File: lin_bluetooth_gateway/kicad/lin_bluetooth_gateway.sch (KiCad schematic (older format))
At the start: 9 parts, among them P1 MOLEX-0431603103, P2 MOLEX-0431603103, P4 CONN_01X03, U1 MCP2050, U2 BL652

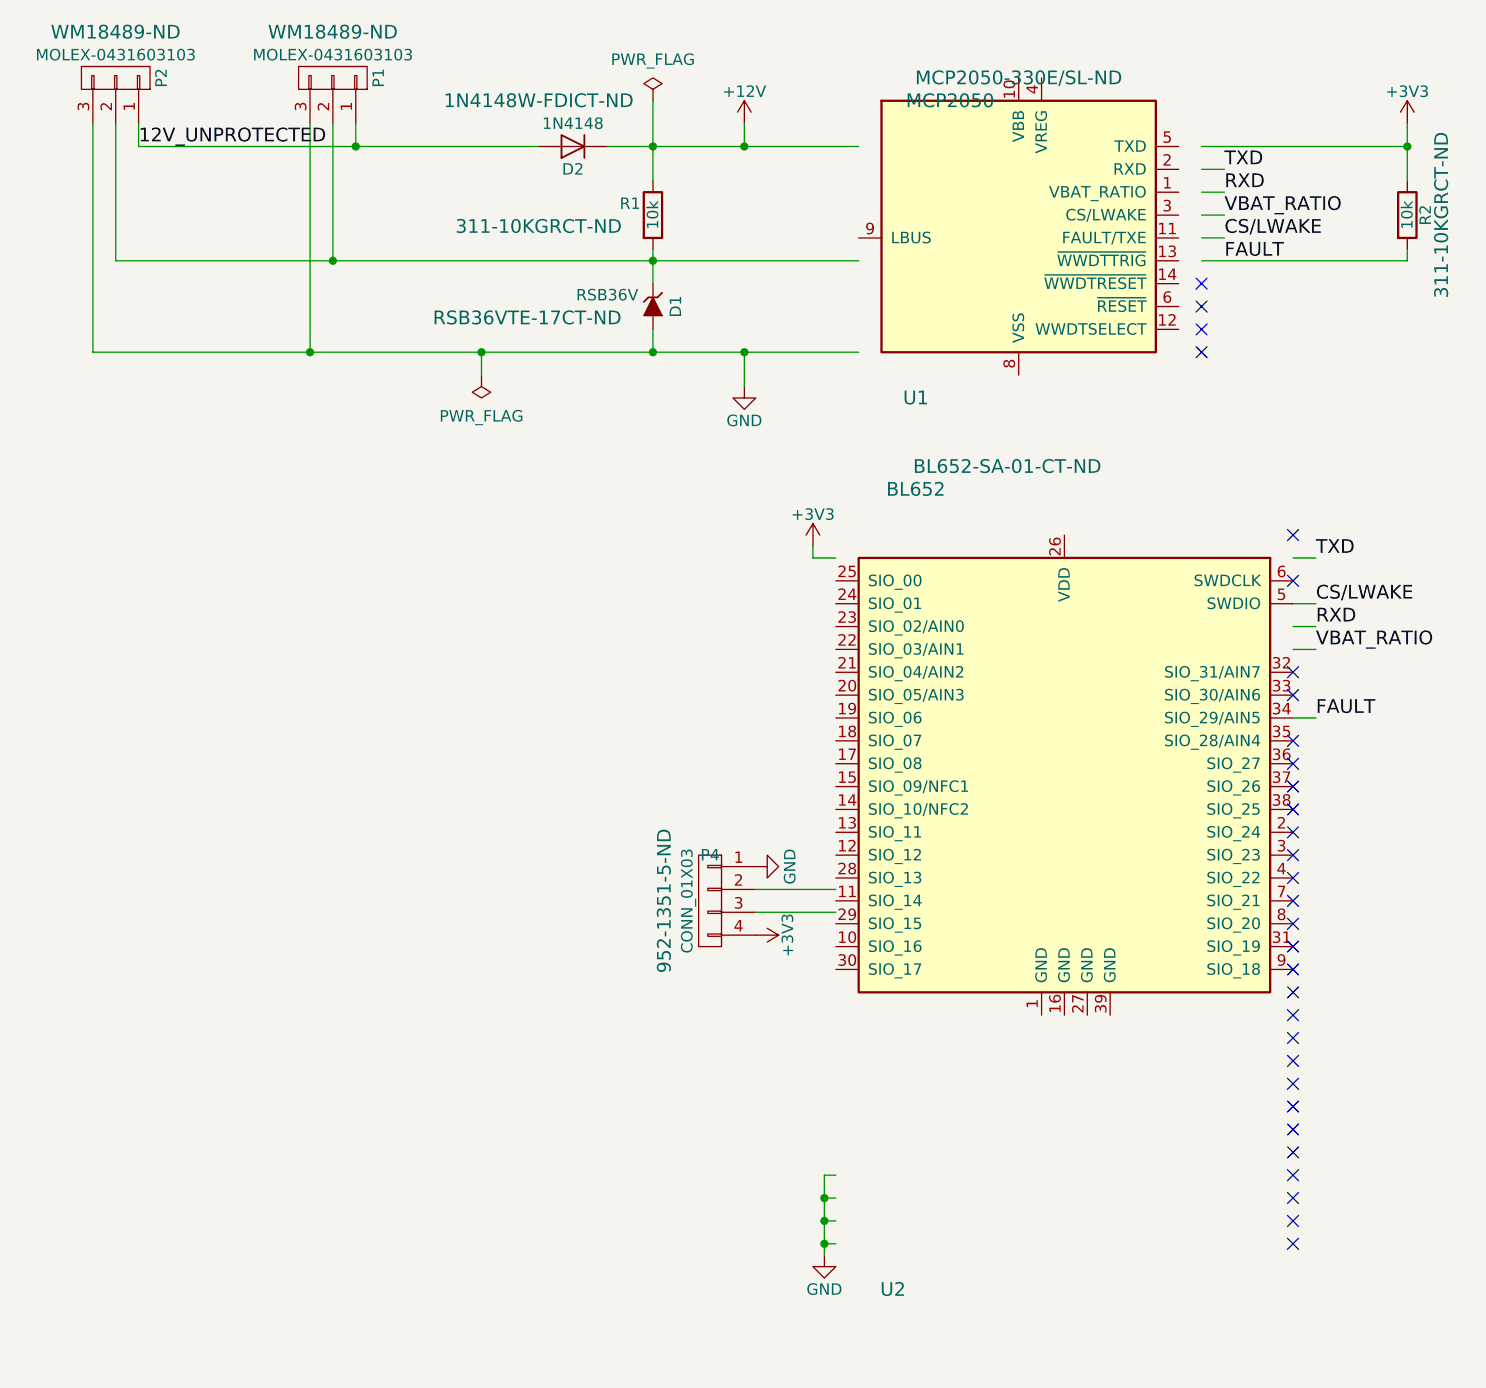
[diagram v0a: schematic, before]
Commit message: Refactoring directories
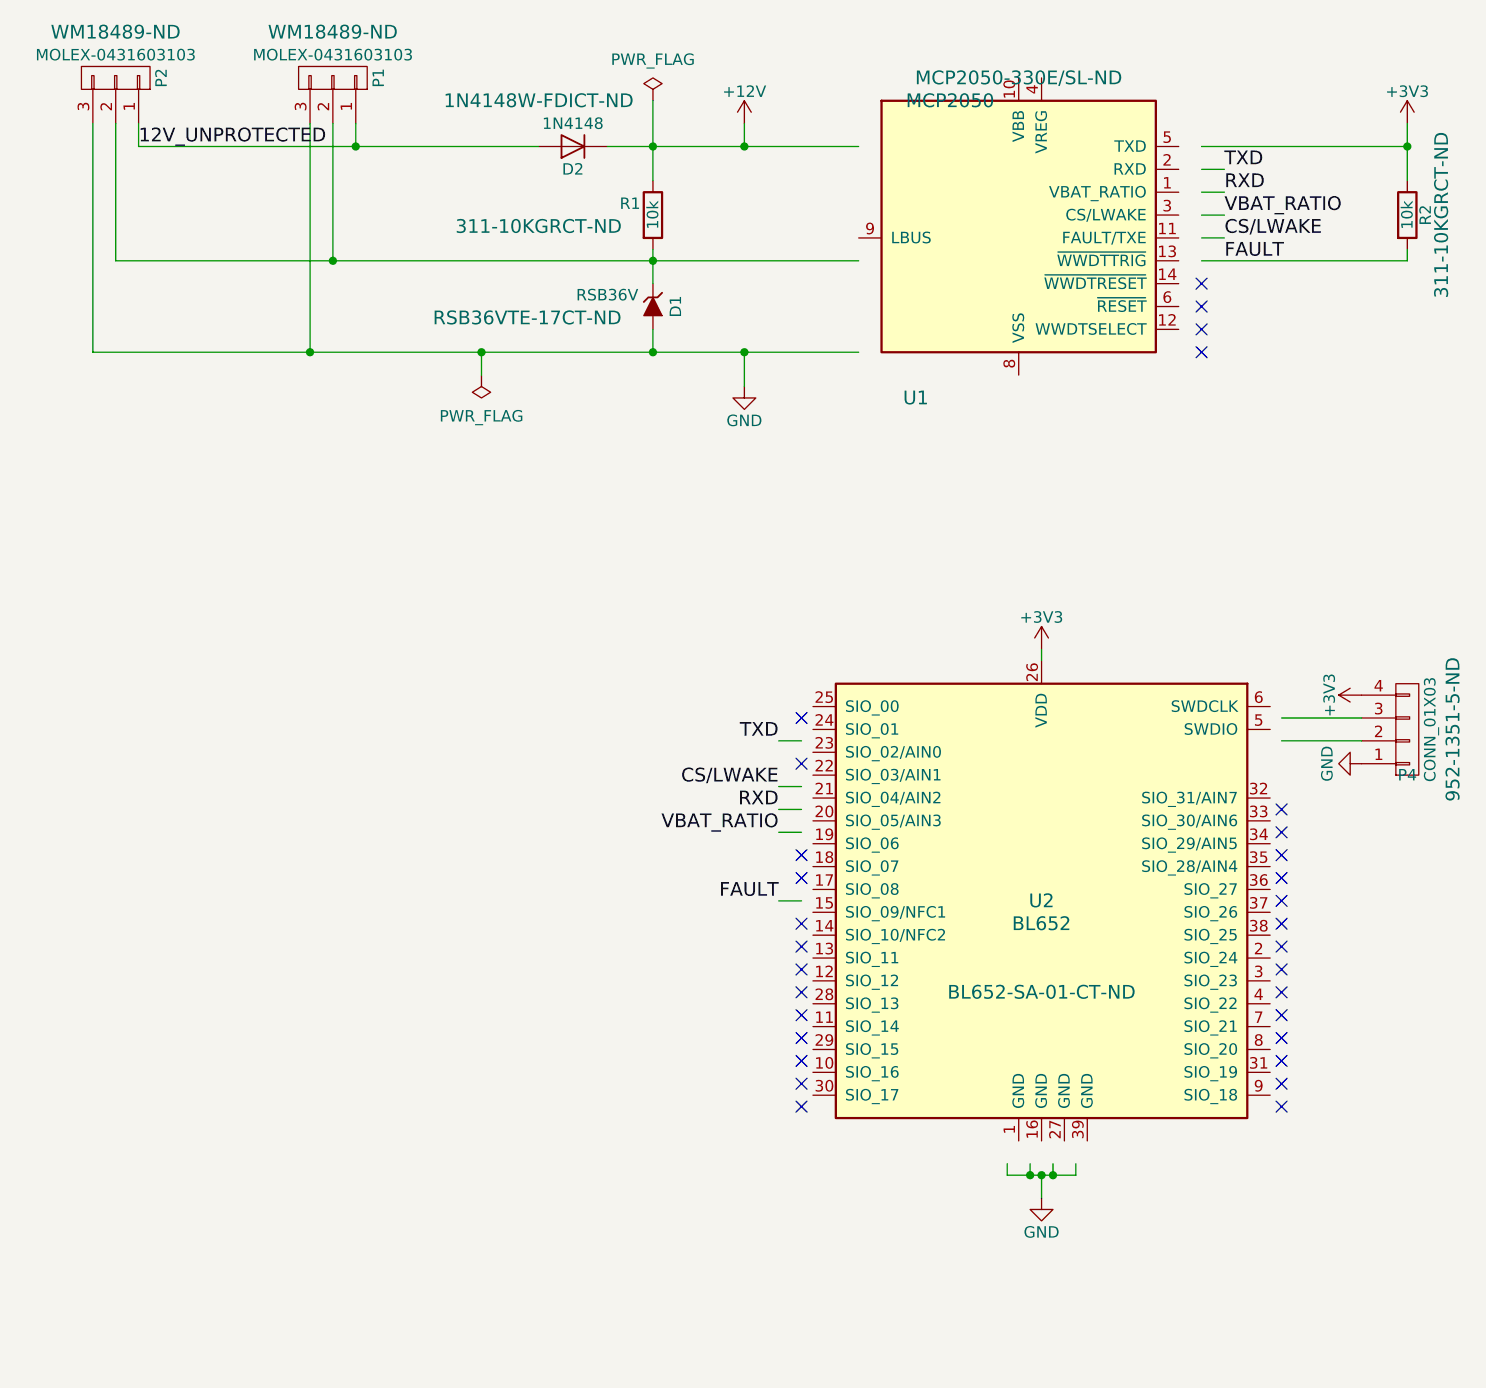
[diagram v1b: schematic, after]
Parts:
- U2: footprint footprints:BL652-SA -> Bluetooth_Modules:Bluetooth_Module_Laird_BL652
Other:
- moved on the sheet: P4, U2
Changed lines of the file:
@@
 LIBS:contrib
 LIBS:valves
-LIBS:bl652
+LIBS:laird
 LIBS:mcp2050
 LIBS:lin_bluetooth_gateway-cache
@@
 L BL652 U2
 U 1 1 5807152B
-P 5550 4250
-F 0 "U2" H 4800 2050 60  0000 C CNN
-F 1 "BL652" H 4900 5550 60  0000 C CNN
-F 2 "footprints:BL652-SA" H 5550 4250 60  0001 C CNN
-F 3 "" H 5550 4250 60  0001 C CNN
-F 4 "BL652-SA-01-CT-ND" H 5300 5650 60  0000 C CNN "DIGIKEY"
-	1    5550 4250
+P 5450 4800
+F 0 "U2" H 5450 4850 60  0000 C CNN
+F 1 "BL652" H 5450 4750 60  0000 C CNN
+F 2 "Bluetooth_Modules:Bluetooth_Module_Laird_BL652" H 5450 4800 60  0001 C CNN
+F 3 "" H 5450 4800 60  0001 C CNN
+F 4 "BL652-SA-01-CT-ND" H 5450 4450 60  0000 C CNN "DIGIKEY"
+	1    5450 4800
 	1    0    0    -1
 $EndComp
@@
 L GND #PWR02
 U 1 1 58071A27
-P 4500 6300
-F 0 "#PWR02" H 4500 6050 50  0001 C CNN
-F 1 "GND" H 4500 6150 50  0000 C CNN
-F 2 "" H 4500 6300 50  0000 C CNN
-F 3 "" H 4500 6300 50  0000 C CNN
-	1    4500 6300
-	1    0    0    -1
-$EndComp
-Wire Wire Line
-	4500 6250 4550 6250
-Wire Wire Line
-	4500 5950 4500 6300
-Wire Wire Line
-	4550 6150 4500 6150
-Connection ~ 4500 6250
-Wire Wire Line
-	4550 6050 4500 6050
-Connection ~ 4500 6150
-Wire Wire Line
-	4550 5950 4500 5950
-Connection ~ 4500 6050
+P 5450 6050
+F 0 "#PWR02" H 5450 5800 50  0001 C CNN
+F 1 "GND" H 5450 5900 50  0000 C CNN
+F 2 "" H 5450 6050 50  0000 C CNN
+F 3 "" H 5450 6050 50  0000 C CNN
+	1    5450 6050
+	1    0    0    -1
+$EndComp
 $Comp
 L MCP2050 U1
@@
 	-1   0    0    1
 $EndComp
-NoConn ~ 6550 3150
-NoConn ~ 6550 3350
-NoConn ~ 6550 3850
-NoConn ~ 6550 3750
-NoConn ~ 6550 4050
-NoConn ~ 6550 4150
-NoConn ~ 6550 4250
-NoConn ~ 6550 4350
-NoConn ~ 6550 4450
-NoConn ~ 6550 4550
-NoConn ~ 6550 4650
-NoConn ~ 6550 4750
-NoConn ~ 6550 4850
-NoConn ~ 6550 4950
-NoConn ~ 6550 5050
-NoConn ~ 6550 5150
-NoConn ~ 6550 5250
-NoConn ~ 6550 5350
-NoConn ~ 6550 5450
 NoConn ~ 6150 2350
 NoConn ~ 6150 2250
 NoConn ~ 6150 2150
 NoConn ~ 6150 2050
-NoConn ~ 6550 5550
-NoConn ~ 6550 5650
 $Comp
 L CONN_01X04 P4
 U 1 1 580874C5
-P 4000 4750
-F 0 "P4" H 4000 4950 50  0000 C CNN
-F 1 "CONN_01X03" V 4100 4750 50  0000 C CNN
-F 2 "Pin_Headers:Pin_Header_Straight_1x04_Pitch2.00mm" H 4000 4750 50  0001 C CNN
-F 3 "" H 4000 4750 50  0000 C CNN
-F 4 "952-1351-5-ND" V 4200 4750 60  0000 C CNN "DIGIKEY"
-	1    4000 4750
-	-1   0    0    -1
+P 7050 4000
+F 0 "P4" H 7050 4200 50  0000 C CNN
+F 1 "CONN_01X03" V 7150 4000 50  0000 C CNN
+F 2 "Pin_Headers:Pin_Header_Straight_1x04_Pitch2.00mm" H 7050 4000 50  0001 C CNN
+F 3 "" H 7050 4000 50  0000 C CNN
+F 4 "952-1351-5-ND" V 7250 4000 60  0000 C CNN "DIGIKEY"
+	1    7050 4000
+	1    0    0    1
 $EndComp
 $Comp
 L GND #PWR06
 U 1 1 5808755D
-P 4200 4600
-F 0 "#PWR06" H 4200 4350 50  0001 C CNN
-F 1 "GND" H 4200 4450 50  0000 C CNN
-F 2 "" H 4200 4600 50  0000 C CNN
-F 3 "" H 4200 4600 50  0000 C CNN
-	1    4200 4600
-	0    -1   -1   0
-$EndComp
-Wire Wire Line
-	4550 4800 4200 4800
-Wire Wire Line
-	4200 4700 4550 4700
+P 6850 4150
+F 0 "#PWR06" H 6850 3900 50  0001 C CNN
+F 1 "GND" H 6850 4000 50  0000 C CNN
+F 2 "" H 6850 4150 50  0000 C CNN
+F 3 "" H 6850 4150 50  0000 C CNN
+	1    6850 4150
+	0    1    1    0
+$EndComp
+Wire Wire Line
+	6500 3950 6850 3950
+Wire Wire Line
+	6850 4050 6500 4050
 $Comp
 L D D2
@@
 L +3V3 #PWR08
 U 1 1 5808A811
-P 4200 4900
-F 0 "#PWR08" H 4200 4750 50  0001 C CNN
-F 1 "+3V3" H 4200 5040 50  0000 C CNN
-F 2 "" H 4200 4900 50  0000 C CNN
-F 3 "" H 4200 4900 50  0000 C CNN
-	1    4200 4900
-	0    1    1    0
+P 6850 3850
+F 0 "#PWR08" H 6850 3700 50  0001 C CNN
+F 1 "+3V3" H 6850 3990 50  0000 C CNN
+F 2 "" H 6850 3850 50  0000 C CNN
+F 3 "" H 6850 3850 50  0000 C CNN
+	1    6850 3850
+	0    -1   -1   0
 $EndComp
 Text Label 6250 1850 0    60   ~ 0
 CS/LWAKE
-Text Label 6650 3450 0    60   ~ 0
+Text Label 4300 4250 2    60   ~ 0
 CS/LWAKE
 $Comp
@@
 Text Label 6250 1950 0    60   ~ 0
 FAULT
-Text Label 6650 3650 0    60   ~ 0
+Text Label 4300 4450 2    60   ~ 0
 VBAT_RATIO
-Text Label 6650 3550 0    60   ~ 0
+Text Label 4300 4350 2    60   ~ 0
 RXD
-Text Label 6650 3250 0    60   ~ 0
+Text Label 4300 4050 2    60   ~ 0
 TXD
 Wire Wire Line
-	6550 3650 6650 3650
-Wire Wire Line
-	6550 3550 6650 3550
-Wire Wire Line
-	6550 3450 6650 3450
-Wire Wire Line
-	6650 3250 6550 3250
+	4400 4450 4300 4450
+Wire Wire Line
+	4400 4350 4300 4350
+Wire Wire Line
+	4400 4250 4300 4250
+Wire Wire Line
+	4300 4050 4400 4050
 $Comp
 L +3V3 #PWR09
 U 1 1 583FE805
-P 4450 3200
-F 0 "#PWR09" H 4450 3050 50  0001 C CNN
-F 1 "+3V3" H 4450 3340 50  0000 C CNN
-F 2 "" H 4450 3200 50  0000 C CNN
-F 3 "" H 4450 3200 50  0000 C CNN
-	1    4450 3200
-	1    0    0    -1
-$EndComp
-Wire Wire Line
-	4550 3250 4450 3250
-Wire Wire Line
-	4450 3250 4450 3200
-NoConn ~ 6550 5750
-NoConn ~ 6550 5850
-NoConn ~ 6550 5950
-NoConn ~ 6550 6050
-NoConn ~ 6550 6150
-NoConn ~ 6550 6250
+P 5450 3650
+F 0 "#PWR09" H 5450 3500 50  0001 C CNN
+F 1 "+3V3" H 5450 3790 50  0000 C CNN
+F 2 "" H 5450 3650 50  0000 C CNN
+F 3 "" H 5450 3650 50  0000 C CNN
+	1    5450 3650
+	1    0    0    -1
+$EndComp
+Wire Wire Line
+	5450 3700 5450 3650
 Text Label 1500 1450 0    60   ~ 0
 12V_UNPROTECTED
@@
 	7050 1950 6150 1950
 Wire Wire Line
-	6550 3950 6650 3950
-Text Label 6650 3950 0    60   ~ 0
+	4400 4750 4300 4750
+Text Label 4300 4750 2    60   ~ 0
 FAULT
+Wire Wire Line
+	5300 5900 5300 5950
+Wire Wire Line
+	5300 5950 5600 5950
+Wire Wire Line
+	5600 5950 5600 5900
+Wire Wire Line
+	5500 5900 5500 5950
+Connection ~ 5500 5950
+Wire Wire Line
+	5400 5900 5400 5950
+Connection ~ 5400 5950
+Wire Wire Line
+	5450 5950 5450 6050
+Connection ~ 5450 5950
+NoConn ~ 6500 4350
+NoConn ~ 6500 4450
+NoConn ~ 6500 4550
+NoConn ~ 6500 4650
+NoConn ~ 6500 4750
+NoConn ~ 6500 4850
+NoConn ~ 6500 4950
+NoConn ~ 6500 5050
+NoConn ~ 6500 5150
+NoConn ~ 6500 5250
+NoConn ~ 6500 5350
+NoConn ~ 6500 5450
+NoConn ~ 6500 5550
+NoConn ~ 6500 5650
+NoConn ~ 4400 3950
+NoConn ~ 4400 4150
+NoConn ~ 4400 4550
+NoConn ~ 4400 4650
+NoConn ~ 4400 4850
+NoConn ~ 4400 4950
+NoConn ~ 4400 5050
+NoConn ~ 4400 5150
+NoConn ~ 4400 5250
+NoConn ~ 4400 5350
+NoConn ~ 4400 5450
+NoConn ~ 4400 5550
+NoConn ~ 4400 5650
 $EndSCHEMATC

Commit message: Using RF_Modules instead of Bluetooth_Modules for BL652
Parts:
- U2: footprint Bluetooth_Modules:Bluetooth_Module_Laird_BL652 -> RF_Modules:Laird_BL652
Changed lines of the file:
@@
 F 0 "U2" H 5450 4850 60  0000 C CNN
 F 1 "BL652" H 5450 4750 60  0000 C CNN
-F 2 "Bluetooth_Modules:Bluetooth_Module_Laird_BL652" H 5450 4800 60  0001 C CNN
+F 2 "RF_Modules:Laird_BL652" H 5450 4800 60  0001 C CNN
 F 3 "" H 5450 4800 60  0001 C CNN
 F 4 "BL652-SA-01-CT-ND" H 5450 4450 60  0000 C CNN "DIGIKEY"
